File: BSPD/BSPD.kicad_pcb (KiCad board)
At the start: 2 copper layers, 55 x 45 mm, 111 parts, among them J2 Conn_02x10_Odd_Even, U1 TLV2371DBV, U10 TLV2371DBV, U13 74LVC1G08, U14 AP2204K-ADJ, U15 AP7375Q-50WR-7, U17 74LVC1G08, U18 74LVC1G08, U2 TLV2371DBV, U3 TLV2371DBV, U4 TLV2371DBV, U5 74LVC1G08, U6 74LVC1G08, U8 TLV2371DBV, U9 TLV2371DBV

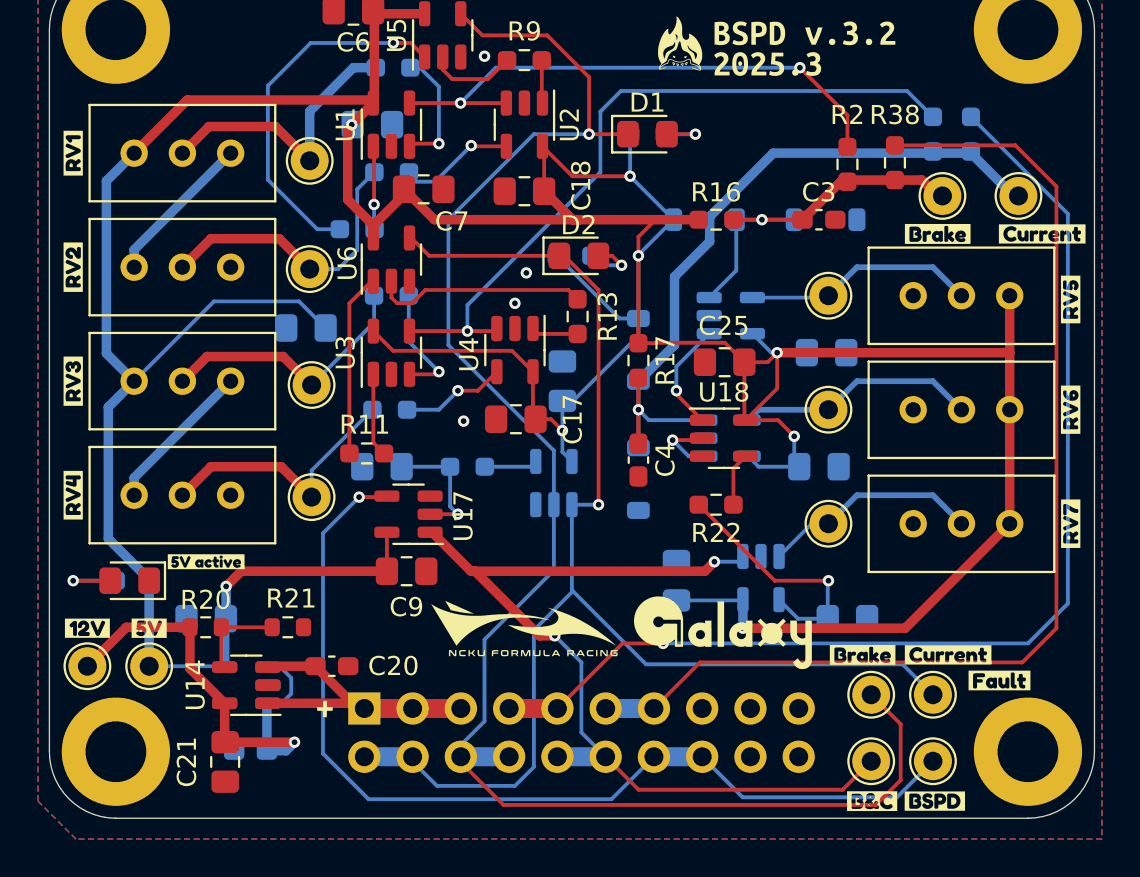
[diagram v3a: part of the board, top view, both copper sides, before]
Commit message: Change some design errors
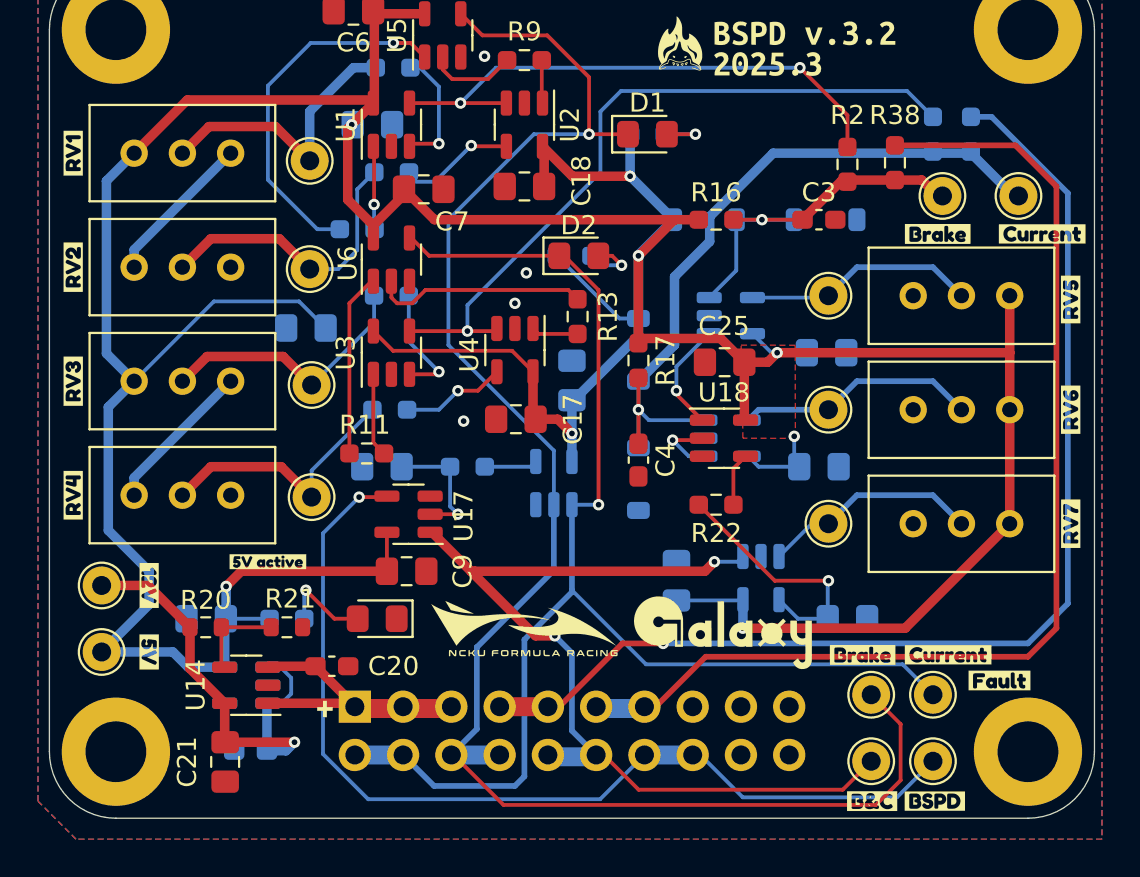
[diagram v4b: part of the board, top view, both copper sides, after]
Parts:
- moved D16 13.2 mm to (134.2, 157.0)
- moved R37 8.34 mm to (129.5, 157.0), turned to 0 degrees
- moved TP16 4.32 mm to (119.8, 155.2)
- moved kibuzzard-67D12A07 3.95 mm to (122.2, 155.2), turned to -90 degrees
- moved kibuzzard-67D12A37 3.25 mm to (128.5, 154.0)
- moved TP8 2.61 mm to (119.8, 158.8)
- moved kibuzzard-67D12A20 1.25 mm to (122.2, 158.8), turned to -90 degrees
- moved J2 0.51 mm to (133.1, 161.6)
- moved C2 0.50 mm to (144.5, 144.5)
- moved C18 0.25 mm to (142.0, 134.2)
- moved R21 0.05 mm to (129.5, 157.4)
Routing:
- net +5V: track 240.7 -> 235.8 mm
- net Brake_init: track 59.4 -> 60.5 mm
- net VDC: track 16.3 -> 15.5 mm
- net Net-(D16-A): track 4.19 -> 4.88 mm
- net +12V: track 24.6 -> 23.9 mm
- net Simultaneous_brake&current: track 48.5 -> 47.9 mm
- added copper zone on F.Cu, net +5V

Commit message: modify some label
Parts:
- removed kibuzzard-67D12B65: G***, kibuzzard-67D12B65
- added G***: LOGO, logo:nckufs_logo_10mm, B.Cu at (145.5, 126.0)
- added G***: LOGO, logo:galaxy_logo_10mm, B.Cu at (158.2, 126.0)
- added kibuzzard-67D16C3B: G***, kibuzzard-67D16C3B, F.Cu at (149.2, 133.2)
- added kibuzzard-67D16C61: G***, kibuzzard-67D16C61, F.Cu at (145.2, 136.2)
- added kibuzzard-67D16C98: G***, kibuzzard-67D16C98, F.Cu at (156.8, 126.5)
- moved kibuzzard-67D12A37 8.75 mm to (136.0, 158.5)
- moved G*** 8.27 mm to (144.2, 157.2)
- moved G*** 5.48 mm to (144.2, 152.5)
- moved C6 2.02 mm to (132.8, 127.0)
- moved C17 0.50 mm to (141.6, 147.0)
- moved G*** 0.50 mm to (150.2, 126.2)

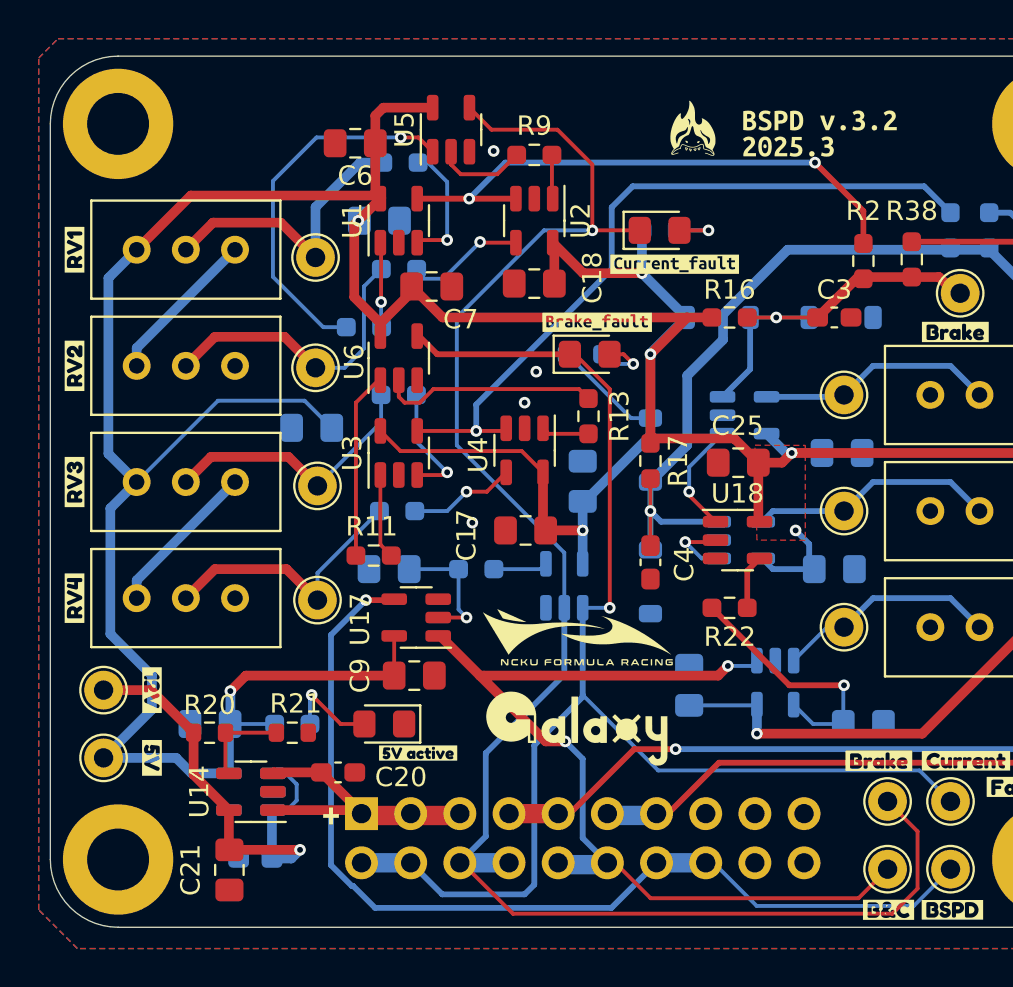
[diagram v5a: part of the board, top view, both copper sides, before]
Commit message: remove 12V LDO
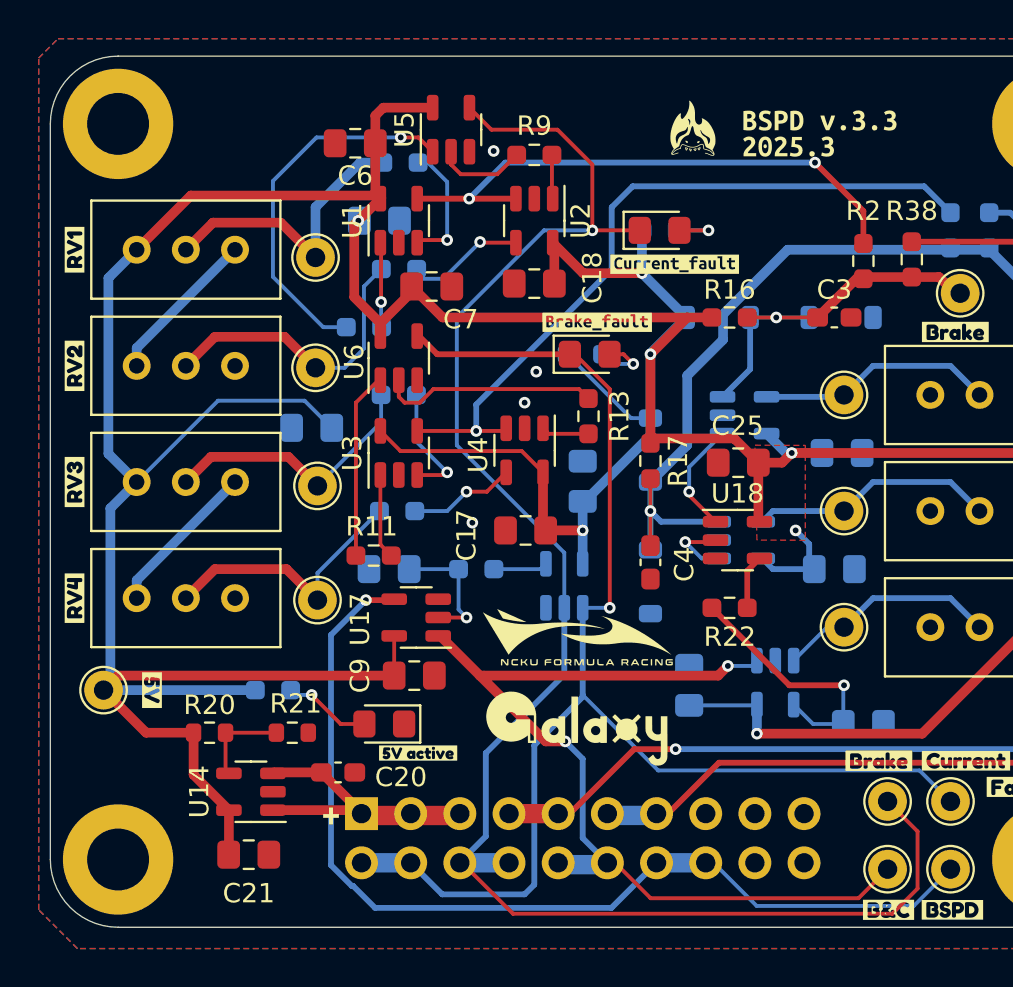
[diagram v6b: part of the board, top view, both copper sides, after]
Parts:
- removed C22: 1u, Capacitor_SMD:C_0603_1608Metric_Pad1.08x0.95mm_HandSolder
- removed C23: 10u, Capacitor_SMD:C_0805_2012Metric_Pad1.18x1.45mm_HandSolder
- removed TP8: TestPoint, TestPoint:TestPoint_THTPad_D2.0mm_Drill1.0mm
- removed U15: AP7375Q-50WR-7, Package_TO_SOT_SMD:SOT-23-5
- removed kibuzzard-67D12A07: G***, kibuzzard-67D12A07
- removed kibuzzard-67D16C98: G***, kibuzzard-67D16C98
- added kibuzzard-67D57EEA: G***, kibuzzard-67D57EEA, F.Cu at (156.8, 126.5)
- U14: value AP2204K-ADJ -> AP7375Q-50WR-7
- moved kibuzzard-67D12A20 3.50 mm to (122.2, 155.2)
- moved R37 2.02 mm to (128.5, 155.2)
- moved C21 1.27 mm to (127.2, 163.8), turned to 0 degrees
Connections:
- C21 pad 1: +12V -> +5V
- R20 pad 1: +12V -> +5V
- TP16 pad 1: +12V -> +5V
- U14 pad 5: +12V -> +5V
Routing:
- net +12V: track 23.9 -> 0.00 mm, vias 1 -> 0
- net +5V: track 236.1 -> 244.5 mm, vias 8 -> 7

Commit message: delete layout
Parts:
- removed C1, C13, C14, C15, C16, C17, C18, C19, C2, C21, C25, C5, C6, C7, C9: 10u, Capacitor_SMD:C_0805_2012Metric_Pad1.18x1.45mm_HandSolder
- removed C20: 1u, Capacitor_SMD:C_0603_1608Metric_Pad1.08x0.95mm_HandSolder
- removed C3, C4: 0.1u, Capacitor_SMD:C_0603_1608Metric_Pad1.08x0.95mm_HandSolder
- removed D1, D16, D2: LED, LED_SMD:LED_0805_2012Metric_Pad1.15x1.40mm_HandSolder
- removed D18, D5, D6, D7: 1N4148W, Diode_SMD:D_SOD-123
- removed G***: LOGO, logo:fire_shark_4mm
- removed G*** (x2): LOGO, logo:nckufs_logo_10mm
- removed G*** (x2): LOGO, logo:galaxy_logo_10mm
- removed H1, H2, H3, H4: MountingHole_Pad, MountingHole:MountingHole_3.2mm_M3_ISO7380_Pad
- removed J2: Conn_02x10_Odd_Even, Connector_PinHeader_2.54mm:PinHeader_2x10_P2.54mm_Vertical
- removed R1, R11, R13, R2, R3, R4, R5, R6, R7, R9: 10k, Resistor_SMD:R_0603_1608Metric_Pad0.98x0.95mm_HandSolder
- removed R10, R37, R8: 470R, Resistor_SMD:R_0603_1608Metric_Pad0.98x0.95mm_HandSolder
- removed R12, R22: 100k, Resistor_SMD:R_0603_1608Metric_Pad0.98x0.95mm_HandSolder
- removed R16, R17: 39k, Resistor_SMD:R_0603_1608Metric_Pad0.98x0.95mm_HandSolder
- removed R20: 866k, Resistor_SMD:R_0603_1608Metric
- removed R21: 100k, Resistor_SMD:R_0603_1608Metric
- removed R38, R39: 100R, Resistor_SMD:R_0603_1608Metric_Pad0.98x0.95mm_HandSolder
- removed RV1, RV2, RV3, RV4, RV5, RV6, RV7: 50k, Potentiometer_THT:Potentiometer_Bourns_3296W_Vertical
- removed TP1, TP10, TP11, TP12, TP13, TP14, TP16, TP2, TP3, TP4, TP5, TP6, TP7, TP9: TestPoint, TestPoint:TestPoint_THTPad_D2.0mm_Drill1.0mm
- removed U1, U10, U2, U3, U4, U8, U9: TLV2371DBV, Package_TO_SOT_SMD:SOT-23-5
- removed U13, U17, U18, U5, U6: 74LVC1G08, Package_TO_SOT_SMD:SOT-23-5
- removed U14: AP7375Q-50WR-7, Package_TO_SOT_SMD:SOT-23-5
- removed kibuzzard-67D12800: G***, kibuzzard-67D12800
- removed kibuzzard-67D1282F: G***, kibuzzard-67D1282F
- removed kibuzzard-67D1286B: G***, kibuzzard-67D1286B
- removed kibuzzard-67D12885: G***, kibuzzard-67D12885
- removed kibuzzard-67D1289B: G***, kibuzzard-67D1289B
- removed kibuzzard-67D128B9: G***, kibuzzard-67D128B9
- removed kibuzzard-67D128E6: G***, kibuzzard-67D128E6
- removed kibuzzard-67D12931: G***, kibuzzard-67D12931
- removed kibuzzard-67D1293D: G***, kibuzzard-67D1293D
- removed kibuzzard-67D12947: G***, kibuzzard-67D12947
- removed kibuzzard-67D12954: G***, kibuzzard-67D12954
- removed kibuzzard-67D12976: G***, kibuzzard-67D12976
- removed kibuzzard-67D1299E: G***, kibuzzard-67D1299E
- removed kibuzzard-67D129F2: G***, kibuzzard-67D129F2
- removed kibuzzard-67D12A20: G***, kibuzzard-67D12A20
- removed kibuzzard-67D12A37: G***, kibuzzard-67D12A37
- removed kibuzzard-67D12B34: G***, kibuzzard-67D12B34
- removed kibuzzard-67D16C3B: G***, kibuzzard-67D16C3B
- removed kibuzzard-67D16C61: G***, kibuzzard-67D16C61
- removed kibuzzard-67D57EEA: G***, kibuzzard-67D57EEA
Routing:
- net +5V: track 244.5 -> 0.00 mm, vias 7 -> 0
- net Current_Limit_Check_out: track 87.6 -> 0.00 mm, vias 1 -> 0
- net Brake_Limit_Check_out: track 70.2 -> 0.00 mm, vias 1 -> 0
- net Brake_init: track 60.5 -> 0.00 mm, vias 1 -> 0
- net Current_init: track 57.7 -> 0.00 mm
- net BSPD: track 51.5 -> 0.00 mm, vias 1 -> 0
- net Simultaneous_brake&current: track 47.9 -> 0.00 mm, vias 2 -> 0
- net brake: track 39.6 -> 0.00 mm, vias 1 -> 0
- net Net-(U3--): track 37.6 -> 0.00 mm, vias 1 -> 0
- net Net-(U1--): track 28.9 -> 0.00 mm, vias 2 -> 0
- net current: track 20.1 -> 0.00 mm, vias 1 -> 0
- net Net-(R7-Pad2): track 19.3 -> 0.00 mm, vias 1 -> 0
- net VDC: track 15.5 -> 0.00 mm
- net Net-(R3-Pad1): track 15.4 -> 0.00 mm
- net Net-(R1-Pad1): track 15.1 -> 0.00 mm
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- removed copper zone on F.Cu, net +5V
- removed copper zone on B.Cu, net GND
- removed copper zone on F.Cu, net GND
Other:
- board outline removed

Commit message: v2025.5
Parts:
- added C1: 10u, Capacitor_SMD:C_0805_2012Metric, F.Cu at (59.4, 66.2)
- added C10: 10u, Capacitor_SMD:C_0805_2012Metric, B.Cu at (178.4, 118.8)
- added C11: 0.1u, Capacitor_SMD:C_0603_1608Metric, B.Cu at (169.8, 83.2)
- added C12: 10u, Capacitor_SMD:C_0805_2012Metric, B.Cu at (165.4, 75.2)
- added C13: 0.1u, Capacitor_SMD:C_0603_1608Metric, F.Cu at (39.1, 54.7)
- added C14: 0.1u, Capacitor_SMD:C_0603_1608Metric, F.Cu at (39.1, 57.2)
- added C15: 0.1u, Capacitor_SMD:C_0603_1608Metric, F.Cu at (39.1, 59.7)
- added C16: 0.1u, Capacitor_SMD:C_0603_1608Metric, F.Cu at (39.1, 62.2)
- added C17: 0.1u, Capacitor_SMD:C_0603_1608Metric, F.Cu at (39.1, 64.7)
- added C18: 0.1u, Capacitor_SMD:C_0603_1608Metric, B.Cu at (150.6, 83.2)
- added C19: 0.1u, Capacitor_SMD:C_0603_1608Metric, F.Cu at (148.8, 91.6)
- added C2: 10u, Capacitor_SMD:C_0805_2012Metric, F.Cu at (59.4, 69.2)
- added C20: 0.1u, Capacitor_SMD:C_0603_1608Metric, B.Cu at (171.5, 91.8)
- added C21: NC, Capacitor_THT:C_Disc_D3.0mm_W1.6mm_P2.50mm, F.Cu at (162.0, 72.2)
- added C25: 10u, Capacitor_SMD:C_0805_2012Metric, F.Cu at (68.2, 72.2)
- added C3: 0.1u, Capacitor_SMD:C_0603_1608Metric, F.Cu at (39.1, 44.6)
- added C4: 0.1u, Capacitor_SMD:C_0603_1608Metric, F.Cu at (39.1, 47.2)
- added C5: 10u, Capacitor_SMD:C_0805_2012Metric, F.Cu at (59.4, 72.2)
- added C6: 10u, Capacitor_SMD:C_0805_2012Metric, F.Cu at (154.6, 76.8)
- added C7: 10u, Capacitor_SMD:C_0805_2012Metric, F.Cu at (63.8, 69.2)
- added C8: 1u, Capacitor_SMD:C_0603_1608Metric, B.Cu at (172.4, 115.9)
- added C9: 10u, Capacitor_SMD:C_0805_2012Metric, F.Cu at (63.8, 72.2)
- added D1: LED, LED_SMD:LED_0805_2012Metric_Pad1.15x1.40mm_HandSolder, F.Cu at (86.4, 31.0)
- added D16: LED, LED_SMD:LED_0805_2012Metric_Pad1.15x1.40mm_HandSolder, F.Cu at (176.6, 120.6)
- added D18: 1N4148W, Diode_SMD:D_SOD-123, F.Cu at (60.2, 28.4)
- added D2: LED, LED_SMD:LED_0805_2012Metric_Pad1.15x1.40mm_HandSolder, F.Cu at (54.9, 21.3)
- added D3: LED, LED_SMD:LED_0805_2012Metric_Pad1.15x1.40mm_HandSolder, F.Cu at (144.0, 34.5)
- added D4: LED, LED_SMD:LED_0805_2012Metric_Pad1.15x1.40mm_HandSolder, F.Cu at (54.9, 27.3)
- added D5: 1N4148W, Diode_SMD:D_SOD-123, F.Cu at (60.2, 18.4)
- added D6: 1N4148W, Diode_SMD:D_SOD-123, F.Cu at (60.2, 21.7)
- added D7: 1N4148W, Diode_SMD:D_SOD-123, F.Cu at (60.2, 25.1)
- added H1: MountingHole_Pad, MountingHole:MountingHole_3.2mm_M3_ISO7380_Pad, F.Cu at (133.5, 121.5)
- added H2: MountingHole_Pad, MountingHole:MountingHole_3.2mm_M3_ISO7380_Pad, F.Cu at (186.5, 121.5)
- added H3: MountingHole_Pad, MountingHole:MountingHole_3.2mm_M3_ISO7380_Pad, F.Cu at (186.5, 73.5)
- added H4: MountingHole_Pad, MountingHole:MountingHole_3.2mm_M3_ISO7380_Pad, F.Cu at (133.5, 73.5)
- added J2: Conn_02x10_Odd_Even, Connector_PinHeader_2.54mm:PinHeader_2x10_P2.54mm_Vertical, B.Cu at (171.4, 122.5)
- added R1: 10k, Resistor_SMD:R_0603_1608Metric, B.Cu at (144.4, 79.0)
- added R10: 1k, Resistor_SMD:R_0603_1608Metric, F.Cu at (47.1, 52.2)
- added R11: 10k, Resistor_SMD:R_0603_1608Metric, F.Cu at (47.1, 54.7)
- added R12: 100R, Resistor_SMD:R_0201_0603Metric, F.Cu at (58.5, 34.1)
- added R13: 10k, Resistor_SMD:R_0603_1608Metric, F.Cu at (47.1, 57.2)
- added R14: 866k, Resistor_SMD:R_0603_1608Metric, B.Cu at (179.2, 115.6)
- added R15: 100k, Resistor_SMD:R_0603_1608Metric, B.Cu at (175.8, 112.6)
- added R16: 39k, Resistor_SMD:R_0603_1608Metric, F.Cu at (47.1, 64.7)
- added R17: 39k, Resistor_SMD:R_0603_1608Metric, F.Cu at (51.1, 44.6)
- added R18: 10k, Resistor_SMD:R_0603_1608Metric, B.Cu at (175.2, 78.8)
- added R19: 1k, Resistor_SMD:R_0603_1608Metric, F.Cu at (143.0, 39.0)
- added R2: 10k, Resistor_SMD:R_0603_1608Metric, F.Cu at (147.0, 84.2)
- added R20: 10k, Resistor_SMD:R_0603_1608Metric, B.Cu at (169.8, 76.8)
- added R21: 10k, Resistor_SMD:R_0603_1608Metric, B.Cu at (173.5, 84.5)
- added R22: 50k, Resistor_SMD:R_0603_1608Metric, F.Cu at (51.1, 57.2)
- added R23: 10k, Resistor_SMD:R_0603_1608Metric, B.Cu at (169.6, 85.2)
- added R24: 10k, Resistor_SMD:R_0603_1608Metric, B.Cu at (175.7, 90.8)
- added R25: 100R, Resistor_SMD:R_0603_1608Metric, B.Cu at (142.0, 121.8)
- added R26: 100R, Resistor_SMD:R_0603_1608Metric, B.Cu at (144.8, 121.8)
- added R27: 100R, Resistor_SMD:R_0603_1608Metric, B.Cu at (139.0, 121.8)
- added R28: 100R, Resistor_SMD:R_0201_0603Metric, F.Cu at (58.5, 35.9)
- added R29: 1k, Resistor_SMD:R_0603_1608Metric, F.Cu at (55.1, 49.7)
- added R3: 10k, Resistor_SMD:R_0603_1608Metric, B.Cu at (144.6, 89.8)
- added R30: 10k, Resistor_SMD:R_0603_1608Metric, B.Cu at (162.2, 80.2)
- added R37: 1k, Resistor_SMD:R_0603_1608Metric_Pad0.98x0.95mm_HandSolder, B.Cu at (175.4, 119.8)
- added R4: 10k, Resistor_SMD:R_0603_1608Metric, F.Cu at (43.1, 59.7)
- added R5: 10k, Resistor_SMD:R_0603_1608Metric, F.Cu at (43.1, 62.2)
- added R6: 10k, Resistor_SMD:R_0603_1608Metric, F.Cu at (43.1, 64.7)
- added R7: 10k, Resistor_SMD:R_0603_1608Metric, F.Cu at (150.8, 77.0)
- added R8: 1k, Resistor_SMD:R_0603_1608Metric, F.Cu at (82.7, 54.1)
- added R9: 10k, Resistor_SMD:R_0603_1608Metric, F.Cu at (150.8, 85.2)
- added RV1: 1M, Potentiometer_THT:Potentiometer_Bourns_3296W_Vertical, F.Cu at (134.6, 81.4)
- added RV2: 1M, Potentiometer_THT:Potentiometer_Bourns_3296W_Vertical, F.Cu at (134.7, 87.6)
- added RV3: 1M, Potentiometer_THT:Potentiometer_Bourns_3296W_Vertical, F.Cu at (26.8, 32.8)
- added RV4: 1M, Potentiometer_THT:Potentiometer_Bourns_3296W_Vertical, F.Cu at (26.8, 39.3)
- added RV5: 1M, Potentiometer_THT:Potentiometer_Bourns_3296W_Vertical, F.Cu at (26.8, 45.7)
- added RV6: 1M, Potentiometer_THT:Potentiometer_Bourns_3296W_Vertical, F.Cu at (24.3, 56.0)
- added RV7: 1M, Potentiometer_THT:Potentiometer_Bourns_3296W_Vertical, F.Cu at (24.3, 62.5)
- added RV8: 1M, Potentiometer_THT:Potentiometer_Bourns_3296W_Vertical, F.Cu at (185.2, 81.8)
- added RV9: 1M, Potentiometer_THT:Potentiometer_Bourns_3296W_Vertical, F.Cu at (185.2, 88.0)
- added TP1: TestPoint, TestPoint:TestPoint_THTPad_D1.5mm_Drill0.7mm, F.Cu at (144.0, 81.6)
- added TP10: TestPoint, TestPoint:TestPoint_THTPad_D1.5mm_Drill0.7mm, F.Cu at (144.8, 118.6)
- added TP11: TestPoint, TestPoint:TestPoint_THTPad_D1.5mm_Drill0.7mm, F.Cu at (139.0, 118.6)
- added TP12: TestPoint, TestPoint:TestPoint_THTPad_D1.5mm_Drill0.7mm, F.Cu at (62.5, 62.9)
- added TP13: TestPoint, TestPoint:TestPoint_THTPad_D1.5mm_Drill0.7mm, F.Cu at (66.0, 45.2)
- added TP14: TestPoint, TestPoint:TestPoint_THTPad_D1.5mm_Drill0.7mm, F.Cu at (66.0, 48.7)
- added TP15: TestPoint, TestPoint:TestPoint_THTPad_D1.5mm_Drill0.7mm, F.Cu at (176.0, 81.8)
- added TP16: TestPoint, TestPoint:TestPoint_THTPad_D1.5mm_Drill0.7mm, F.Cu at (176.0, 88.0)
- added TP17: TestPoint, TestPoint:TestPoint_THTPad_D1.5mm_Drill0.7mm, F.Cu at (66.0, 59.4)
- added TP18: TestPoint, TestPoint:TestPoint_THTPad_D1.5mm_Drill0.7mm, F.Cu at (66.0, 62.9)
- added TP2: TestPoint, TestPoint:TestPoint_THTPad_D1.5mm_Drill0.7mm, F.Cu at (144.2, 87.6)
- added TP3: TestPoint, TestPoint:TestPoint_THTPad_D1.5mm_Drill0.7mm, F.Cu at (58.9, 52.3)
- added TP4: TestPoint, TestPoint:TestPoint_THTPad_D1.5mm_Drill0.7mm, F.Cu at (58.9, 55.8)
- added TP5: TestPoint, TestPoint:TestPoint_THTPad_D1.5mm_Drill0.7mm, F.Cu at (58.9, 59.4)
- added TP6: TestPoint, TestPoint:TestPoint_THTPad_D1.5mm_Drill0.7mm, F.Cu at (58.9, 62.9)
- added TP7: TestPoint, TestPoint:TestPoint_THTPad_D1.5mm_Drill0.7mm, F.Cu at (62.5, 45.2)
- added TP8: TestPoint, TestPoint:TestPoint_THTPad_D1.5mm_Drill0.7mm, F.Cu at (179.2, 112.4)
- added TP9: TestPoint, TestPoint:TestPoint_THTPad_D1.5mm_Drill0.7mm, F.Cu at (142.0, 118.6)
- added U1: TLV2371DBV, Package_TO_SOT_SMD:SOT-23-5, F.Cu at (148.8, 80.2)
- added U10: TLV2371DBV, Package_TO_SOT_SMD:SOT-23-5, F.Cu at (44.8, 32.3)
- added U11: TLV2371DBV, Package_TO_SOT_SMD:SOT-23-5, B.Cu at (171.4, 80.1)
- added U12: 74LVC1G08, Package_TO_SOT_SMD:SOT-23-5, B.Cu at (165.5, 78.5)
- added U13: 74LVC1G08, Package_TO_SOT_SMD:SOT-23-5, F.Cu at (50.0, 18.9)
- added U14: TLV2371DBV, Package_TO_SOT_SMD:SOT-23-5, B.Cu at (171.5, 88.5)
- added U15: 74LVC1G08, Package_TO_SOT_SMD:SOT-23-5, F.Cu at (50.0, 27.8)
- added U17: 74LVC1G08, Package_TO_SOT_SMD:SOT-23-5, F.Cu at (50.0, 32.3)
- added U18: 74LVC1G08, Package_TO_SOT_SMD:SOT-23-5, F.Cu at (50.0, 36.7)
- added U2: TLV2371DBV, Package_TO_SOT_SMD:SOT-23-5, F.Cu at (148.8, 88.5)
- added U3: TLV2371DBV, Package_TO_SOT_SMD:SOT-23-5, F.Cu at (39.6, 27.8)
- added U4: TLV2371DBV, Package_TO_SOT_SMD:SOT-23-5, F.Cu at (39.6, 32.3)
- added U5: 74LVC1G08, Package_TO_SOT_SMD:SOT-23-5, F.Cu at (154.1, 79.8)
- added U6: 74LVC1G08, Package_TO_SOT_SMD:SOT-23-5, F.Cu at (39.6, 41.2)
- added U7: AP2204K-ADJ, Package_TO_SOT_SMD:SOT-23-5, B.Cu at (175.8, 115.6)
- added U8: TLV2371DBV, Package_TO_SOT_SMD:SOT-23-5, F.Cu at (44.8, 23.4)
- added U9: TLV2371DBV, Package_TO_SOT_SMD:SOT-23-5, F.Cu at (44.8, 27.8)
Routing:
- net current_init: track 0.00 -> 10.7 mm, vias 0 -> 1
- net BSE_R_init: track 0.00 -> 7.67 mm
- net BSE_L_init: track 0.00 -> 6.61 mm, vias 0 -> 1
- net Net-(U1--): track 0.00 -> 5.99 mm
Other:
- board outline added: 60 x 55 mm
